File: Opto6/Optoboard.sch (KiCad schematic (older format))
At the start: 51 parts, among them J1 S1 Connector, J2 S2 Connector, J3 S3 Connector, J4 S4 Connector, J6 S5 Connector, J7 S6 Connector, P1 CONN_01X08, Q1 IRLR024NPBF, U1 6N135, U2 6N135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

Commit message: Added output files for both version
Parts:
- removed 5V_IN1: Screw_Terminal_01x02, Connectors_Terminal_Blocks:TerminalBlock_4UCON_19963_02x3.5mm_Straight, symbol Screw_Terminal_01x02
- removed Q1: IRLR024NPBF, TO_SOT_Packages_SMD:TO-252-2, symbol IRLB8721PBF
- added U7: L7805, TO_SOT_Packages_SMD:TO-252-2Lead, symbol L7805
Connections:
- wire segments 143 -> 141
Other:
- note added: "5V FROM REGULATOR\n\n"
- note removed: "5V IN WITH MOSFET PROTECTION\n\n"
- moved on the sheet: 12V_IN1, C1, D1

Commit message: Added files
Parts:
- added P2: CONN_01X02, Pin_Headers:Pin_Header_Straight_1x02, symbol CONN_01X02
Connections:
- net +5V: now also P2.2 (P2); no longer P1.1 (P1)
- new net: P1.1 (P1), P2.1 (P1)
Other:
- note added: "P2 is a jumper which if you enable and have 5V \non it, it will act as the powersupply for 5V logic"
- moved on the sheet: 12V_IN1, C1, D1

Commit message: Modified to 3.3V and 5V compatibility
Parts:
- removed U7: L7805, TO_SOT_Packages_SMD:TO-252-2Lead, symbol L7805
- added U7: LM2937ET-3.3, TO_SOT_Packages_SMD:SOT-223, symbol SPX2920T-3.3
- 12V_IN1: footprint Connectors_Terminal_Blocks:TerminalBlock_4UCON_19963_02x3.5mm_Straight -> Connectors_Terminal_Blocks:TerminalBlock_Pheonix_MKDS1.5-2pol
- U1, U2, U3, U4, U5, U6: symbol 6N135 -> 6N135-RESCUE-Optoboard
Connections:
- net +12V: now also U7.1 (VI)
- net GND: now also U7.2 (GND)
- net +5V renamed +3V3
- net +3V3: now also U7.3 (VO)
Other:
- note added: "P2 is a jumper which if you enable and have 3V3 \non it, it will act as the powersupply for 3V3 logic"
- note removed: "P2 is a jumper which if you enable and have 5V \non it, it will act as the powersupply for 5V logic"
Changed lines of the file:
@@
 EESchema Schematic File Version 2
+LIBS:Optoboard-rescue
 LIBS:power
 LIBS:device
 LIBS:switches
 LIBS:relays
+LIBS:motors
 LIBS:transistors
 LIBS:conn
@@
 $EndDescr
 $Comp
-L 6N135 U1
+L 6N135-RESCUE-Optoboard U1
 U 1 1 59C8B84D
 P 2150 1300
@@
 F 0 "12V_IN1" H 7650 1100 50  0000 C CNN
 F 1 "Screw_Terminal_01x02" V 7900 900 50  0000 C CNN
-F 2 "Connectors_Terminal_Blocks:TerminalBlock_4UCON_19963_02x3.5mm_Straight" H 7800 1000 50  0001 C CNN
+F 2 "Connectors_Terminal_Blocks:TerminalBlock_Pheonix_MKDS1.5-2pol" H 7800 1000 50  0001 C CNN
 F 3 "" H 7800 1000 50  0001 C CNN
 	1    7800 1000
@@
 F 3 "" H 7800 3050 50  0001 C CNN
 	1    7800 3050
-	1    0    0    -1
-$EndComp
-$Comp
-L +5V #PWR32
-U 1 1 59C8D32B
-P 7800 2600
-F 0 "#PWR32" H 7800 2450 50  0001 C CNN
-F 1 "+5V" H 7800 2740 50  0000 C CNN
-F 2 "" H 7800 2600 50  0001 C CNN
-F 3 "" H 7800 2600 50  0001 C CNN
-	1    7800 2600
 	1    0    0    -1
 $EndComp
@@
 NoConn ~ 2450 1200
 $Comp
-L +5V #PWR7
-U 1 1 59C9090A
-P 2600 1050
-F 0 "#PWR7" H 2600 900 50  0001 C CNN
-F 1 "+5V" H 2600 1190 50  0000 C CNN
-F 2 "" H 2600 1050 50  0001 C CNN
-F 3 "" H 2600 1050 50  0001 C CNN
-	1    2600 1050
-	1    0    0    -1
-$EndComp
-$Comp
 L GND #PWR8
 U 1 1 59C90BB5
@@
 F 3 "" H 2600 1550 50  0001 C CNN
 	1    2600 1550
-	1    0    0    -1
-$EndComp
-$Comp
-L +5V #PWR25
-U 1 1 59C91360
-P 5800 2400
-F 0 "#PWR25" H 5800 2250 50  0001 C CNN
-F 1 "+5V" H 5800 2540 50  0000 C CNN
-F 2 "" H 5800 2400 50  0001 C CNN
-F 3 "" H 5800 2400 50  0001 C CNN
-	1    5800 2400
 	1    0    0    -1
 $EndComp
@@
 S1
 $Comp
-L 6N135 U3
+L 6N135-RESCUE-Optoboard U3
 U 1 1 59C95703
 P 4350 1250
@@
 NoConn ~ 4650 1150
 $Comp
-L +5V #PWR19
-U 1 1 59C95753
-P 4800 1000
-F 0 "#PWR19" H 4800 850 50  0001 C CNN
-F 1 "+5V" H 4800 1140 50  0000 C CNN
-F 2 "" H 4800 1000 50  0001 C CNN
-F 3 "" H 4800 1000 50  0001 C CNN
-	1    4800 1000
-	1    0    0    -1
-$EndComp
-$Comp
 L GND #PWR20
 U 1 1 59C95759
@@
 S3
 $Comp
-L 6N135 U2
+L 6N135-RESCUE-Optoboard U2
 U 1 1 59C95B88
 P 2150 2900
@@
 NoConn ~ 2450 2800
 $Comp
-L +5V #PWR9
-U 1 1 59C95BD8
-P 2600 2650
-F 0 "#PWR9" H 2600 2500 50  0001 C CNN
-F 1 "+5V" H 2600 2790 50  0000 C CNN
-F 2 "" H 2600 2650 50  0001 C CNN
-F 3 "" H 2600 2650 50  0001 C CNN
-	1    2600 2650
-	1    0    0    -1
-$EndComp
-$Comp
 L GND #PWR10
 U 1 1 59C95BDE
@@
 S2
 $Comp
-L 6N135 U4
+L 6N135-RESCUE-Optoboard U4
 U 1 1 59C95BE5
 P 4350 2850
@@
 NoConn ~ 4650 2750
 $Comp
-L +5V #PWR21
-U 1 1 59C95C35
-P 4800 2600
-F 0 "#PWR21" H 4800 2450 50  0001 C CNN
-F 1 "+5V" H 4800 2740 50  0000 C CNN
-F 2 "" H 4800 2600 50  0001 C CNN
-F 3 "" H 4800 2600 50  0001 C CNN
-	1    4800 2600
-	1    0    0    -1
-$EndComp
-$Comp
 L GND #PWR22
 U 1 1 59C95C3B
@@
 	1    0    0    -1
 $EndComp
-$Comp
-L +5V #PWR27
-U 1 1 59C992CF
-P 5900 850
-F 0 "#PWR27" H 5900 700 50  0001 C CNN
-F 1 "+5V" H 5900 990 50  0000 C CNN
-F 2 "" H 5900 850 50  0001 C CNN
-F 3 "" H 5900 850 50  0001 C CNN
-	1    5900 850
-	1    0    0    -1
-$EndComp
 Wire Wire Line
 	5900 900  5900 850
@@
 	6550 500  6550 3750
 Wire Wire Line
-	7300 2950 7850 2950
+	7200 2950 7850 2950
 Wire Wire Line
 	7800 2950 7800 3050
@@
 12V INPUT WITH DIODE PROTECTION
 $Comp
-L 6N135 U5
+L 6N135-RESCUE-Optoboard U5
 U 1 1 59E789CC
 P 2150 4550
@@
 NoConn ~ 2450 4450
 $Comp
-L +5V #PWR11
-U 1 1 59E78A1C
-P 2600 4300
-F 0 "#PWR11" H 2600 4150 50  0001 C CNN
-F 1 "+5V" H 2600 4440 50  0000 C CNN
-F 2 "" H 2600 4300 50  0001 C CNN
-F 3 "" H 2600 4300 50  0001 C CNN
-	1    2600 4300
-	1    0    0    -1
-$EndComp
-$Comp
 L GND #PWR12
 U 1 1 59E78A22
@@
 S5
 $Comp
-L 6N135 U6
+L 6N135-RESCUE-Optoboard U6
 U 1 1 59E78A29
 P 4350 4500
@@
 NoConn ~ 4650 4400
 $Comp
-L +5V #PWR23
-U 1 1 59E78A79
-P 4800 4250
-F 0 "#PWR23" H 4800 4100 50  0001 C CNN
-F 1 "+5V" H 4800 4390 50  0000 C CNN
-F 2 "" H 4800 4250 50  0001 C CNN
-F 3 "" H 4800 4250 50  0001 C CNN
-	1    4800 4250
-	1    0    0    -1
-$EndComp
-$Comp
 L GND #PWR24
 U 1 1 59E78A7F
@@
 Text GLabel 5800 3200 0    60   Input ~ 0
 S6
-$Comp
-L L7805 U7
-U 1 1 5A004D8A
-P 7300 2650
-F 0 "U7" H 7150 2775 50  0000 C CNN
-F 1 "L7805" H 7300 2775 50  0000 L CNN
-F 2 "TO_SOT_Packages_SMD:TO-252-2Lead" H 7325 2500 50  0001 L CIN
-F 3 "" H 7300 2600 50  0001 C CNN
-	1    7300 2650
-	1    0    0    -1
-$EndComp
 Wire Wire Line
 	7600 2650 7850 2650
-Wire Wire Line
-	7000 2650 6950 2650
-Wire Wire Line
-	6950 2650 6950 2600
 $Comp
 L +12V #PWR29
 U 1 1 5A0056DA
-P 6950 2600
-F 0 "#PWR29" H 6950 2450 50  0001 C CNN
-F 1 "+12V" H 6950 2740 50  0000 C CNN
-F 2 "" H 6950 2600 50  0001 C CNN
-F 3 "" H 6950 2600 50  0001 C CNN
-	1    6950 2600
+P 6750 2600
+F 0 "#PWR29" H 6750 2450 50  0001 C CNN
+F 1 "+12V" H 6750 2740 50  0000 C CNN
+F 2 "" H 6750 2600 50  0001 C CNN
+F 3 "" H 6750 2600 50  0001 C CNN
+	1    6750 2600
 	1    0    0    -1
 $EndComp
@@
 	5800 2450 5800 2400
 Text Notes 600  5900 0    118  ~ 0
-P2 is a jumper which if you enable and have 5V \non it, it will act as the powersupply for 5V logic
+P2 is a jumper which if you enable and have 3V3 \non it, it will act as the powersupply for 3V3 logic
+$Comp
+L +3.3V #PWR32
+U 1 1 5A5F3F44
+P 7800 2600
+F 0 "#PWR32" H 7800 2450 50  0001 C CNN
+F 1 "+3.3V" H 7800 2740 50  0000 C CNN
+F 2 "" H 7800 2600 50  0001 C CNN
+F 3 "" H 7800 2600 50  0001 C CNN
+	1    7800 2600
+	1    0    0    -1
+$EndComp
+$Comp
+L +3.3V #PWR27
+U 1 1 5A5F430C
+P 5900 850
+F 0 "#PWR27" H 5900 700 50  0001 C CNN
+F 1 "+3.3V" H 5900 990 50  0000 C CNN
+F 2 "" H 5900 850 50  0001 C CNN
+F 3 "" H 5900 850 50  0001 C CNN
+	1    5900 850
+	1    0    0    -1
+$EndComp
+$Comp
+L +3.3V #PWR25
+U 1 1 5A5F46CD
+P 5800 2400
+F 0 "#PWR25" H 5800 2250 50  0001 C CNN
+F 1 "+3.3V" H 5800 2540 50  0000 C CNN
+F 2 "" H 5800 2400 50  0001 C CNN
+F 3 "" H 5800 2400 50  0001 C CNN
+	1    5800 2400
+	1    0    0    -1
+$EndComp
+$Comp
+L +3.3V #PWR19
+U 1 1 5A5F4930
+P 4800 1000
+F 0 "#PWR19" H 4800 850 50  0001 C CNN
+F 1 "+3.3V" H 4800 1140 50  0000 C CNN
+F 2 "" H 4800 1000 50  0001 C CNN
+F 3 "" H 4800 1000 50  0001 C CNN
+	1    4800 1000
+	1    0    0    -1
+$EndComp
+$Comp
+L +3.3V #PWR21
+U 1 1 5A5F4C5B
+P 4800 2600
+F 0 "#PWR21" H 4800 2450 50  0001 C CNN
+F 1 "+3.3V" H 4800 2740 50  0000 C CNN
+F 2 "" H 4800 2600 50  0001 C CNN
+F 3 "" H 4800 2600 50  0001 C CNN
+	1    4800 2600
+	1    0    0    -1
+$EndComp
+$Comp
+L +3.3V #PWR23
+U 1 1 5A5F4E28
+P 4800 4250
+F 0 "#PWR23" H 4800 4100 50  0001 C CNN
+F 1 "+3.3V" H 4800 4390 50  0000 C CNN
+F 2 "" H 4800 4250 50  0001 C CNN
+F 3 "" H 4800 4250 50  0001 C CNN
+	1    4800 4250
+	1    0    0    -1
+$EndComp
+$Comp
+L +3.3V #PWR11
+U 1 1 5A5F521B
+P 2600 4300
+F 0 "#PWR11" H 2600 4150 50  0001 C CNN
+F 1 "+3.3V" H 2600 4440 50  0000 C CNN
+F 2 "" H 2600 4300 50  0001 C CNN
+F 3 "" H 2600 4300 50  0001 C CNN
+	1    2600 4300
+	1    0    0    -1
+$EndComp
+$Comp
+L +3.3V #PWR9
+U 1 1 5A5F54E2
+P 2600 2650
+F 0 "#PWR9" H 2600 2500 50  0001 C CNN
+F 1 "+3.3V" H 2600 2790 50  0000 C CNN
+F 2 "" H 2600 2650 50  0001 C CNN
+F 3 "" H 2600 2650 50  0001 C CNN
+	1    2600 2650
+	1    0    0    -1
+$EndComp
+$Comp
+L +3.3V #PWR7
+U 1 1 5A5F5871
+P 2600 1050
+F 0 "#PWR7" H 2600 900 50  0001 C CNN
+F 1 "+3.3V" H 2600 1190 50  0000 C CNN
+F 2 "" H 2600 1050 50  0001 C CNN
+F 3 "" H 2600 1050 50  0001 C CNN
+	1    2600 1050
+	1    0    0    -1
+$EndComp
+$Comp
+L SPX2920T-3.3 U7
+U 1 1 5A5F67AF
+P 7200 2700
+F 0 "U7" H 7200 2950 50  0000 C CNN
+F 1 "LM2937ET-3.3" H 7200 2900 50  0000 C CNN
+F 2 "TO_SOT_Packages_SMD:SOT-223" H 7200 2800 50  0001 C CIN
+F 3 "" H 7200 2700 50  0001 C CNN
+	1    7200 2700
+	1    0    0    -1
+$EndComp
+Wire Wire Line
+	6750 2650 6800 2650
+Wire Wire Line
+	6750 2650 6750 2600
 $EndSCHEMATC

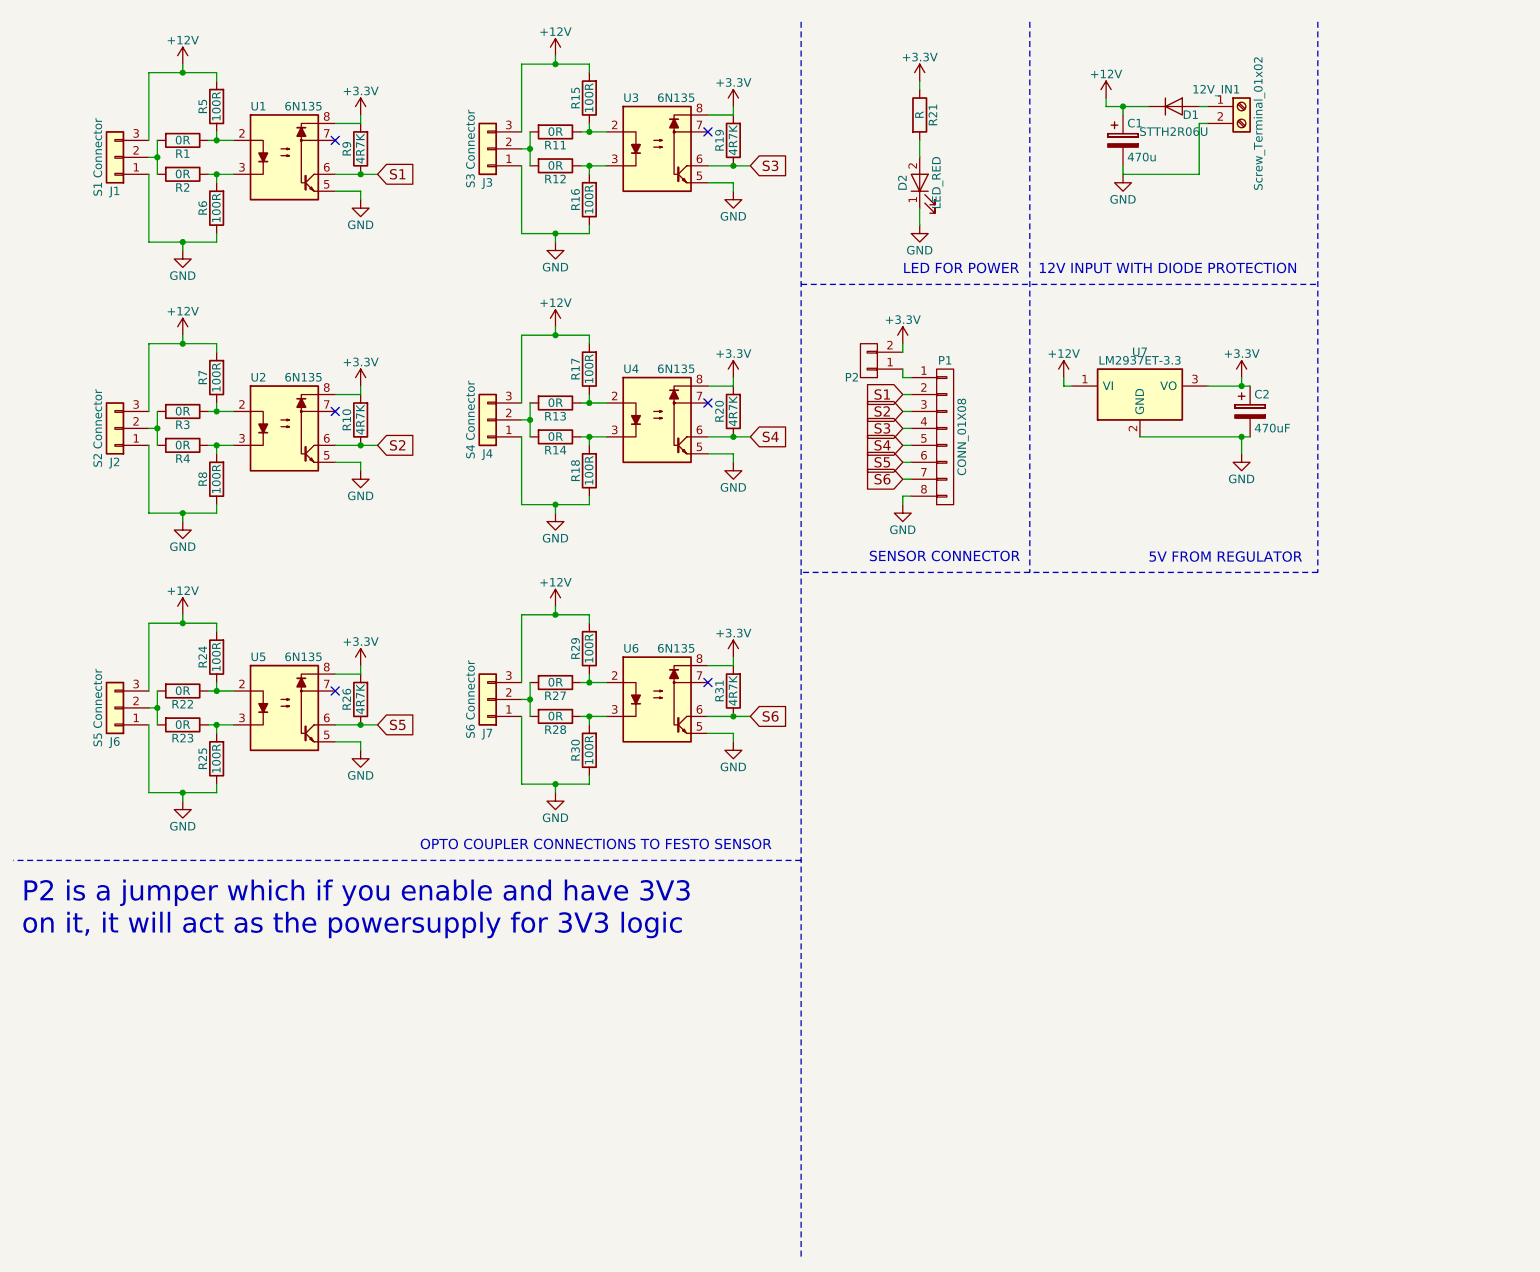
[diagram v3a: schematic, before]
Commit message: Added pdf and images
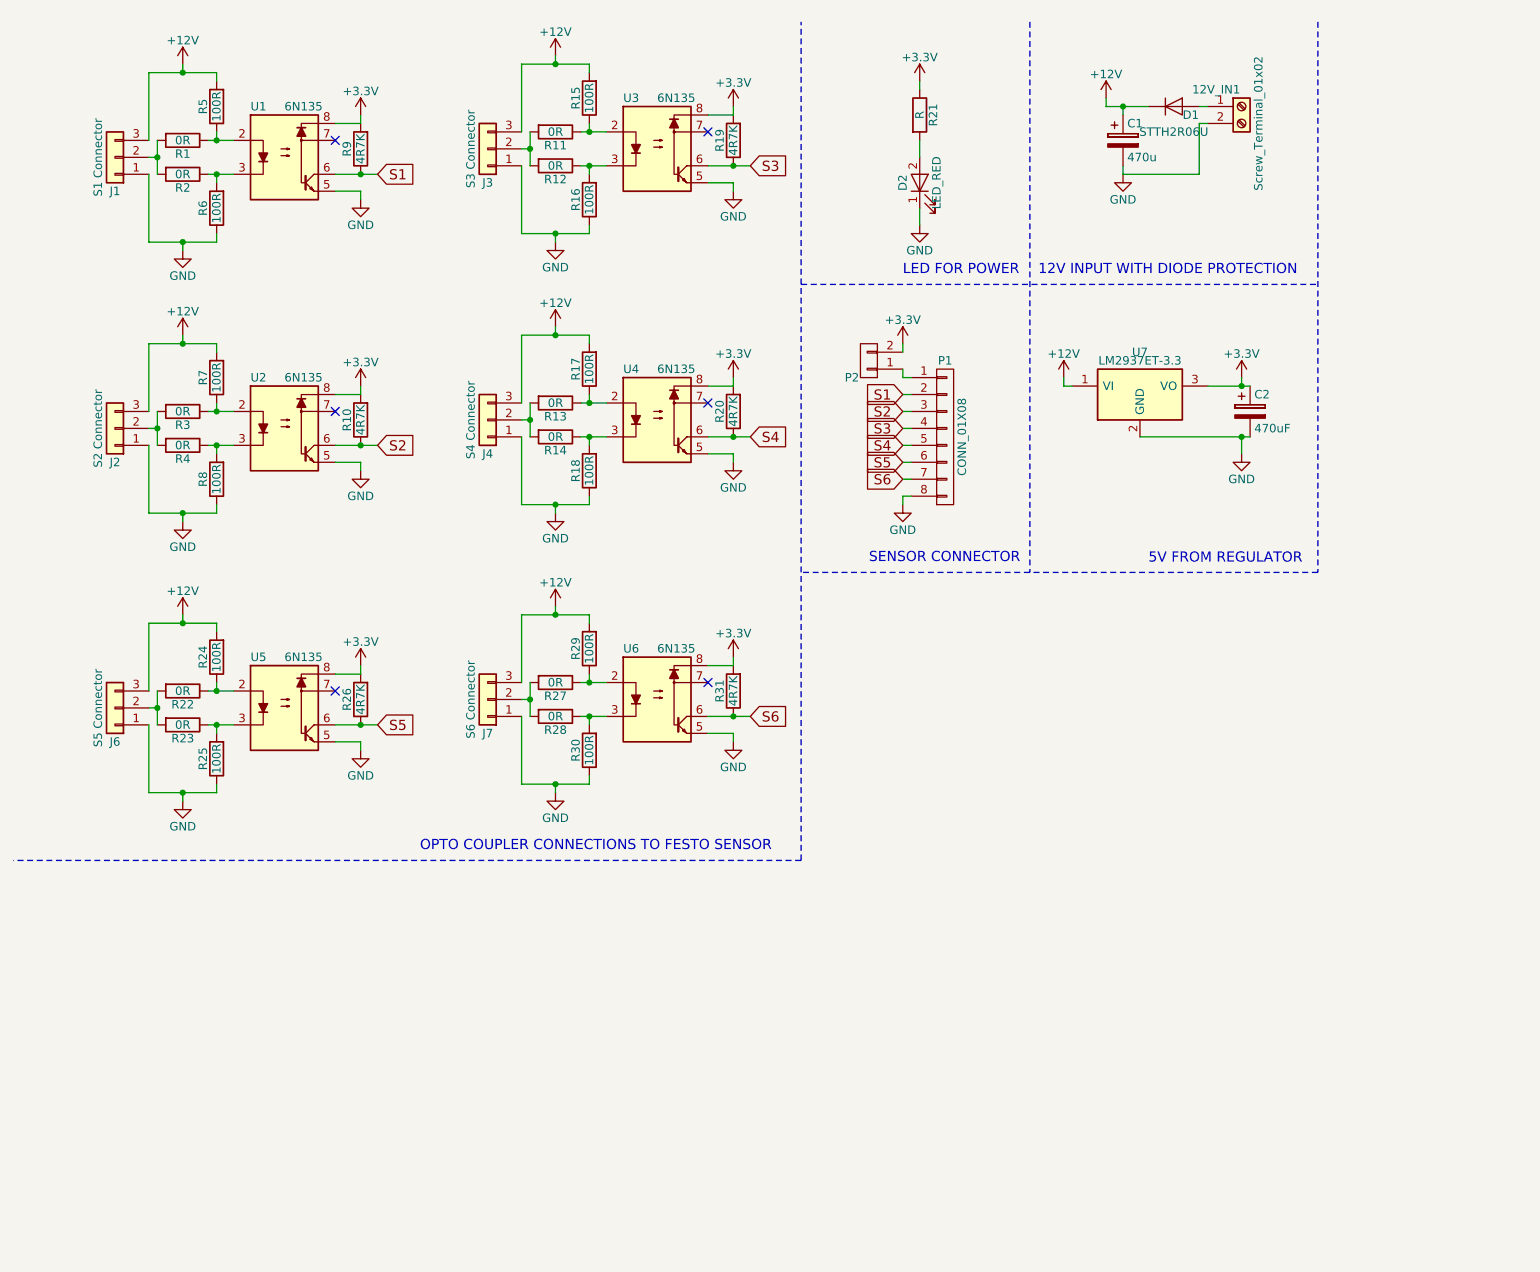
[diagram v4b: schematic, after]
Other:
- note removed: "P2 is a jumper which if you enable and have 3V3 \non it, it will act as the powersupply for 3V3 logic"
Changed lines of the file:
@@
 Sheet 1 1
 Title "Opto isolator board for festo sensors"
-Date "2017-09-30"
+Date "2018-02-10"
 Rev "1"
 Comp "Electropioneer"
@@
 Wire Wire Line
 	5900 900  5900 850
-Wire Notes Line
-	5200 500  5200 7800
 Wire Notes Line
 	5200 2050 8250 2050
@@
 Wire Wire Line
 	5800 2450 5800 2400
-Text Notes 600  5900 0    118  ~ 0
-P2 is a jumper which if you enable and have 3V3 \non it, it will act as the powersupply for 3V3 logic
 $Comp
 L +3.3V #PWR32
@@
 Wire Wire Line
 	6750 2650 6750 2600
+Wire Notes Line
+	5200 5450 5200 500
 $EndSCHEMATC

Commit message: Updated the regulator and some small modifs
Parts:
- added C3, C4: 100n, Capacitors_SMD:C_0805, symbol C
- added MK1, MK2: Mounting_Hole, Mounting_Holes:MountingHole_3.2mm_M3_Pad_Via, symbol Mounting_Hole
- C1: value 470u -> 100u
- C2: value 470uF -> 100u
- U7: value LM2937ET-3.3 -> LM7805; footprint TO_SOT_Packages_SMD:SOT-223 -> TO_SOT_Packages_SMD:TO-252-2Lead
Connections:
- net +12V: now also C3.1
- net GND: now also C3.2, C4.2
- net +3V3 renamed VCC
- net VCC: now also C4.1
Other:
- note added: "Mounting holes"
- moved on the sheet: C2, U7
